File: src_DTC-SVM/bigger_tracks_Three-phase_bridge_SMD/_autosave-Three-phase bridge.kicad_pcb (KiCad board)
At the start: 2 copper layers, 401.6 x 318 mm, 105 parts, among them M1 MCP6022-I/P, M2 MCP6022-I/P, P1 CONN_1, P10 CONN_1, P11 CONN_1, P12 CONN_1, P13 CONN_1, P2 POWER_FUSE, P3 CONN_2, P4 CONN_1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

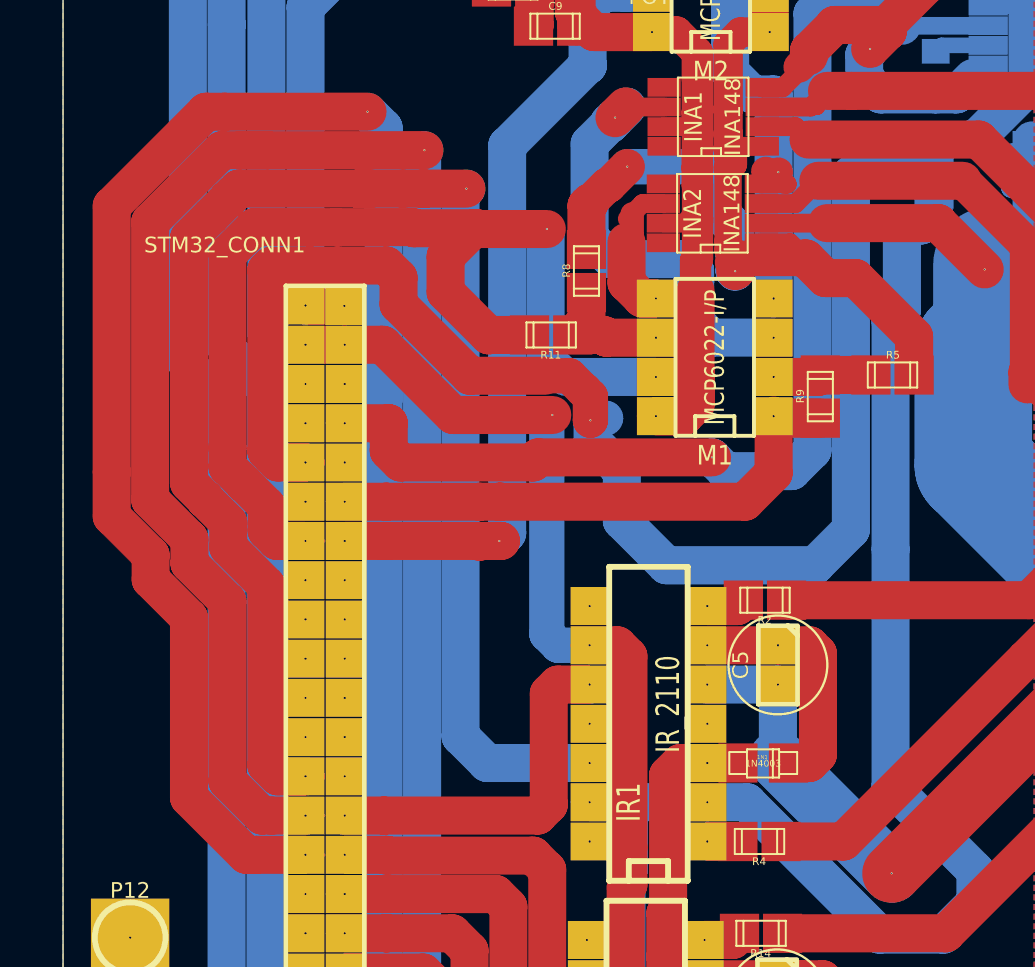
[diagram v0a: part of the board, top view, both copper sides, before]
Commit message: Modulos originales de libreria de Sebastian
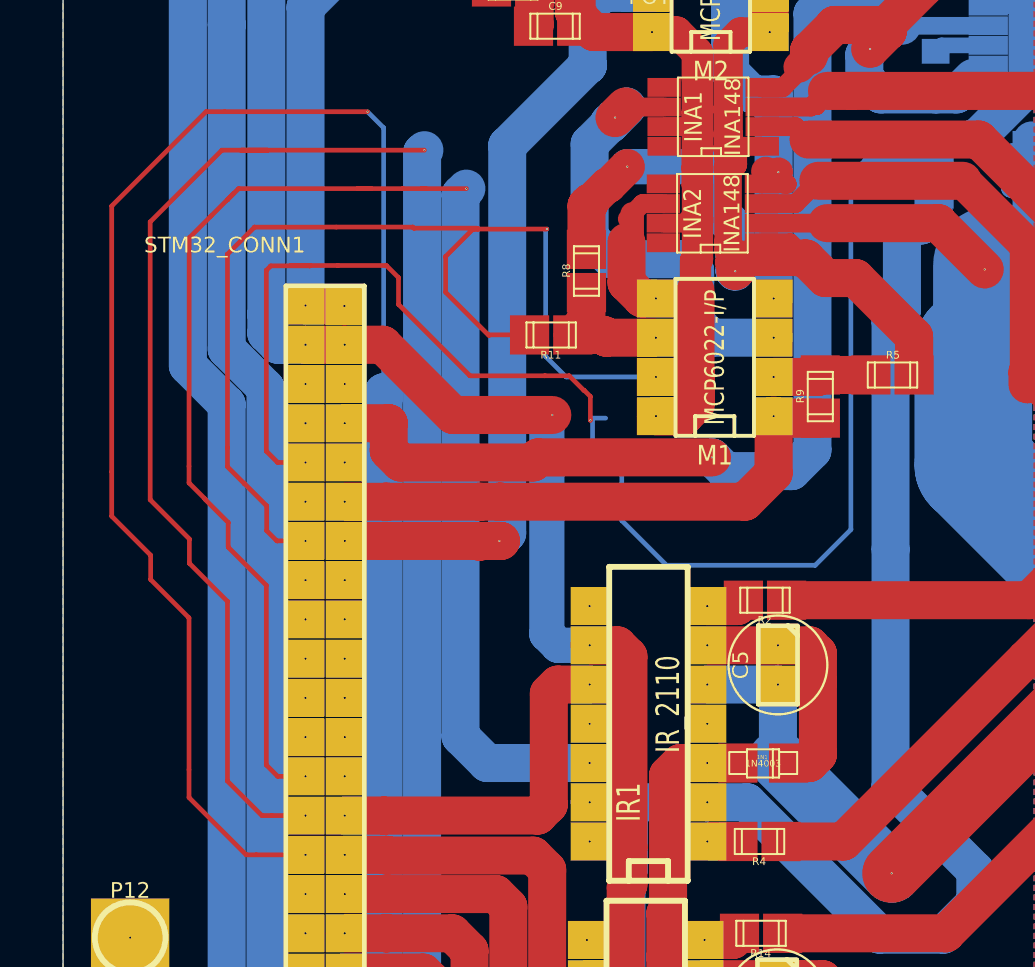
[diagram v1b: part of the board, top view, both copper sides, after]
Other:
- net class pistas12mil added: clearance 0.254, trace_width 0.3048, via_dia 0.127, via_drill 0.1016
